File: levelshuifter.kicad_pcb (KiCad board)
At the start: 2 copper layers, 55 x 153 mm, 30 parts, among them J1 Screw_Terminal_01x02, J2 Conn_02x20_Odd_Even, J3 Conn_02x08_Odd_Even, J4 Conn_02x08_Odd_Even, J5 Conn_02x08_Odd_Even, U1 LM1117-3.3, U2 74LVC8T245PW, U3 74LVC8T245PW, U4 74LVC8T245PW, U5 L7805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

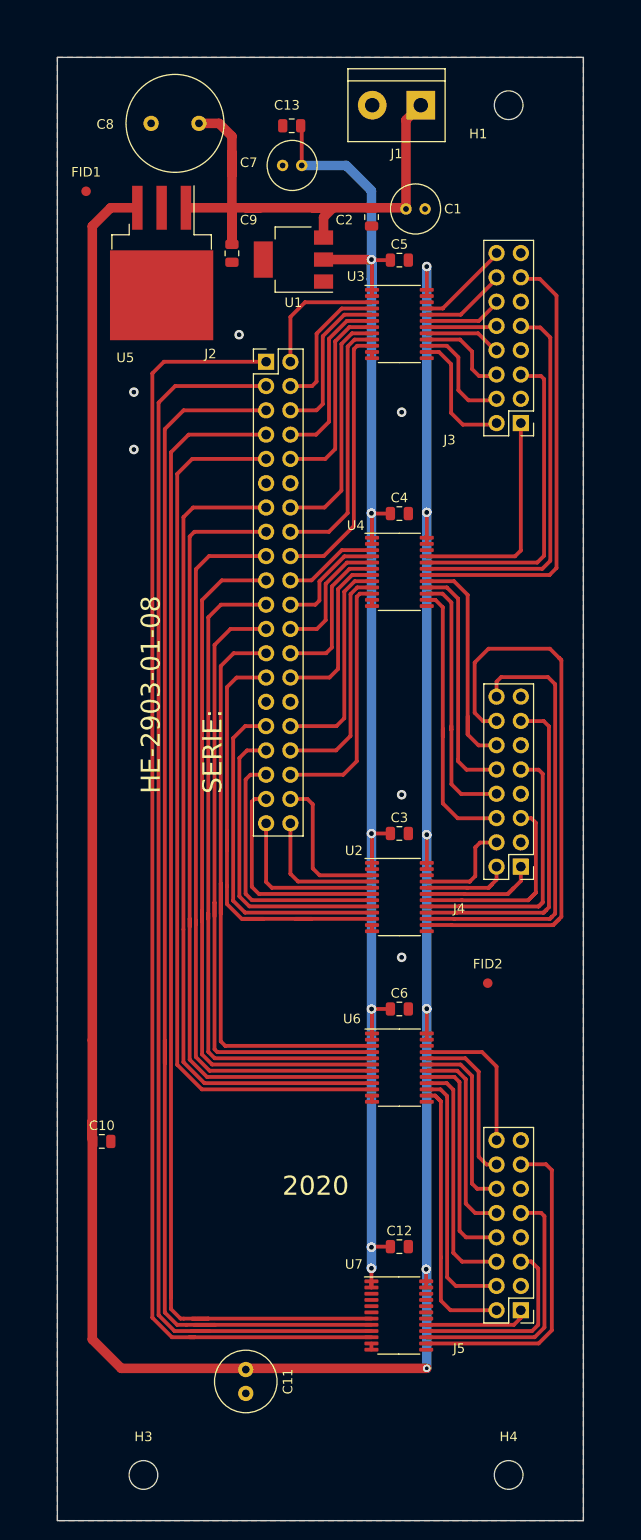
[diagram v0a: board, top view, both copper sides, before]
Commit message: sugerencias agregadas parcialmente
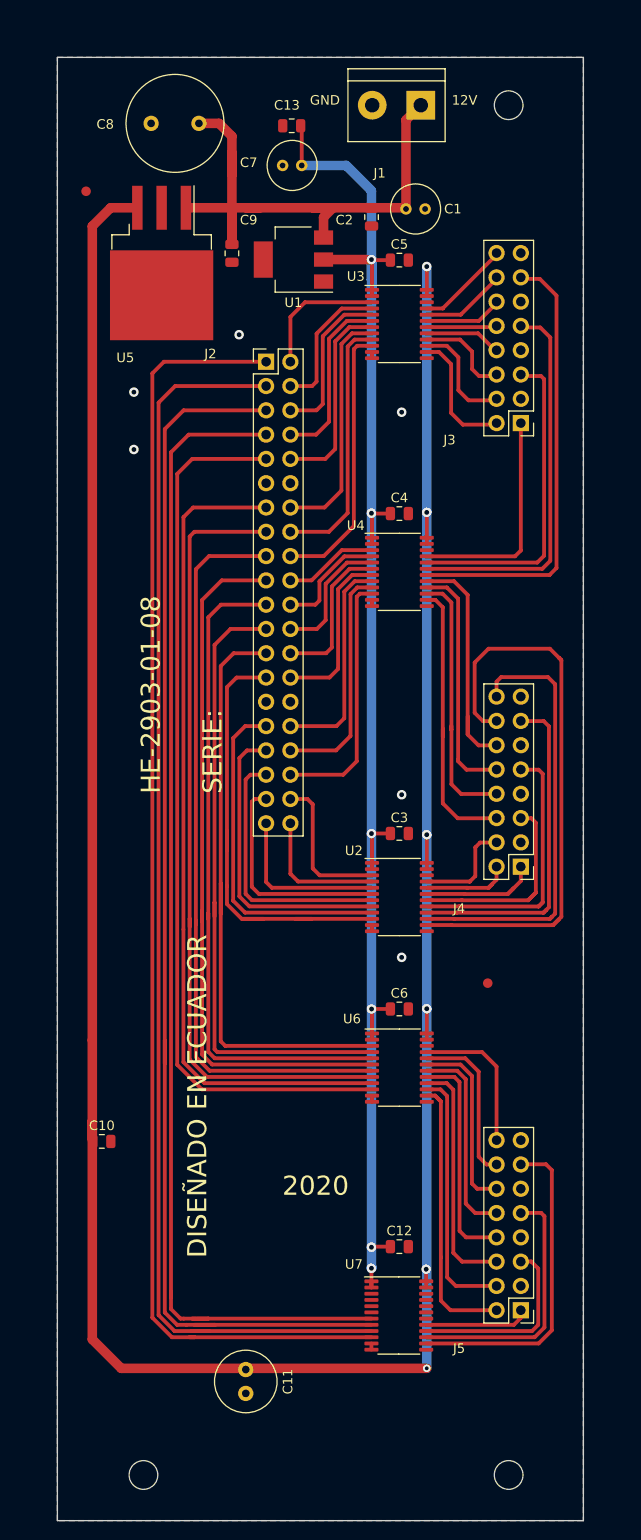
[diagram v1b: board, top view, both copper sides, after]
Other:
- board text added: "12V"
- board text added: "DISEÑADO EN ECUADOR"
- board text added: "GND"

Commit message: cambios 2
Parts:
- removed H4: MountingHole, MountingHole:MountingHole_3mm
- moved H3 7.22 mm to (35.0, 167.0)
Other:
- board size 55 x 153 mm -> 55 x 145 mm
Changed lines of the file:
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@@
   (general
     (thickness 1.6)
-    (drawings 13)
+    (drawings 12)
     (tracks 524)
     (zones 0)
-    (modules 30)
+    (modules 29)
     (nets 87)
   )
@@
   )
   (module MountingHole:MountingHole_3mm (layer F.Cu)
-    (at 73.185 174.224999)
-    (descr "Mounting Hole 3mm, no annular")
-    (tags "mounting hole 3mm no annular")
-    (attr virtual)
-    (fp_text reference H4 (at 0 -4) (layer F.SilkS) hide
-      (effects (font (size 1 1) (thickness 0.15)))
-    )
-    (fp_text value MountingHole (at 0 4) (layer F.Fab)
-      (effects (font (size 1 1) (thickness 0.15)))
-    )
-    (fp_circle (center 0 0) (end 3 0) (layer Cmts.User) (width 0.15))
-    (fp_circle (center 0 0) (end 3.25 0) (layer F.CrtYd) (width 0.05))
-    (fp_text user %R (at 0.3 0) (layer F.Fab)
-      (effects (font (size 1 1) (thickness 0.15)))
-    )
-    (pad 1 np_thru_hole circle (at 0 0) (size 3 3) (drill 3) (layers *.Cu *.Mask))
-  )
-  (module MountingHole:MountingHole_3mm (layer F.Cu)
-    (at 35 174.224999)
+    (at 35 167.005)
     (descr "Mounting Hole 3mm, no annular")
     (tags "mounting hole 3mm no annular")
@@
     )
   )
-  (gr_text "GND\n" (at 53.975 30.48) (layer F.SilkS)
-    (effects (font (size 1 1) (thickness 0.15)))
-  )
-  (gr_text "12V\n" (at 68.58 30.48) (layer F.SilkS)
-    (effects (font (size 1 1) (thickness 0.15)))
-  )
-  (gr_text "DISEÑADO EN ECUADOR" (at 40.64 134.62 90) (layer F.SilkS)
-    (effects (font (size 2 2) (thickness 0.15)))
-  )
-  (gr_text 2020 (at 53 144) (layer F.SilkS)
-    (effects (font (size 2 2) (thickness 0.15)))
-  )
-  (gr_text "HE-2903-01-08\n\nSERIE:" (at 39 103 90) (layer F.SilkS)
-    (effects (font (size 2 2) (thickness 0.15)) (justify left))
-  )
-  (gr_text "Fabricante seleccionado: Microcircuitos (Colombia)\nLimitaciones:\nhttps://pcbmicrocircuitos.com/wp-content/uploads/2016/12/medidas-minimas-microcircuitos-1.jpg\nDistancias:\n\ncobre-cobre: 0.203mm\nagujero-agujero:0.5mm\npads-serigraf:0.23mm\n\nAncho:\n\nPista:0.203mm\nVia:0.25mm\nSerigrafía:0.23mm\n\n" (at 102 50) (layer Dwgs.User)
-    (effects (font (size 2 2) (thickness 0.15)) (justify left))
-  )
   (dimension 55 (width 0.15) (layer Dwgs.User)
     (gr_text "55,000 mm" (at 53.5 18.7) (layer Dwgs.User)
@@
     (arrow2b (pts (xy 26 20) (xy 27.126504 19.413579)))
   )
-  (dimension 153 (width 0.15) (layer Dwgs.User)
-    (gr_text "153,000 mm" (at 92.3 102.5 270) (layer Dwgs.User)
-      (effects (font (size 1 1) (thickness 0.15)))
-    )
-    (feature1 (pts (xy 81 179) (xy 91.586421 179)))
-    (feature2 (pts (xy 81 26) (xy 91.586421 26)))
-    (crossbar (pts (xy 91 26) (xy 91 179)))
-    (arrow1a (pts (xy 91 179) (xy 90.413579 177.873496)))
-    (arrow1b (pts (xy 91 179) (xy 91.586421 177.873496)))
-    (arrow2a (pts (xy 91 26) (xy 90.413579 27.126504)))
-    (arrow2b (pts (xy 91 26) (xy 91.586421 27.126504)))
-  )
-  (gr_line (start 26 179) (end 26 26) (layer Edge.Cuts) (width 0.05))
-  (gr_line (start 81 178) (end 81 179) (layer Edge.Cuts) (width 0.05))
-  (gr_line (start 81 26) (end 81 178) (layer Edge.Cuts) (width 0.05))
+  (dimension 145 (width 0.15) (layer Dwgs.User)
+    (gr_text "145,000 mm" (at 87.3 98.5 270) (layer Dwgs.User)
+      (effects (font (size 1 1) (thickness 0.15)))
+    )
+    (feature1 (pts (xy 81 171) (xy 86.586421 171)))
+    (feature2 (pts (xy 81 26) (xy 86.586421 26)))
+    (crossbar (pts (xy 86 26) (xy 86 171)))
+    (arrow1a (pts (xy 86 171) (xy 85.413579 169.873496)))
+    (arrow1b (pts (xy 86 171) (xy 86.586421 169.873496)))
+    (arrow2a (pts (xy 86 26) (xy 85.413579 27.126504)))
+    (arrow2b (pts (xy 86 26) (xy 86.586421 27.126504)))
+  )
+  (gr_line (start 26 171) (end 26 26) (layer Edge.Cuts) (width 0.05))
+  (gr_line (start 26 171) (end 81 171) (layer Edge.Cuts) (width 0.05))
+  (gr_line (start 81 26) (end 81 171) (layer Edge.Cuts) (width 0.05))
   (gr_line (start 26 26) (end 81 26) (layer Edge.Cuts) (width 0.05))
-  (gr_line (start 81 179) (end 26 179) (layer Edge.Cuts) (width 0.05))
+  (gr_text "GND\n" (at 53.975 30.48) (layer F.SilkS)
+    (effects (font (size 1 1) (thickness 0.15)))
+  )
+  (gr_text "12V\n" (at 68.58 30.48) (layer F.SilkS)
+    (effects (font (size 1 1) (thickness 0.15)))
+  )
+  (gr_text "DISEÑADO EN ECUADOR" (at 40.64 134.62 90) (layer F.SilkS)
+    (effects (font (size 2 2) (thickness 0.15)))
+  )
+  (gr_text 2020 (at 53 144) (layer F.SilkS)
+    (effects (font (size 2 2) (thickness 0.15)))
+  )
+  (gr_text "HE-2903-01-08\n\nSERIE:" (at 39 103 90) (layer F.SilkS)
+    (effects (font (size 2 2) (thickness 0.15)) (justify left))
+  )
+  (gr_text "Fabricante seleccionado: Microcircuitos (Colombia)\nLimitaciones:\nhttps://pcbmicrocircuitos.com/wp-content/uploads/2016/12/medidas-minimas-microcircuitos-1.jpg\nDistancias:\n\ncobre-cobre: 0.203mm\nagujero-agujero:0.5mm\npads-serigraf:0.23mm\n\nAncho:\n\nPista:0.203mm\nVia:0.25mm\nSerigrafía:0.23mm\n\n" (at 102 50) (layer Dwgs.User)
+    (effects (font (size 2 2) (thickness 0.15)) (justify left))
+  )
   (segment (start 44.25 45.55) (end 44.25 42) (width 1) (layer F.Cu) (net 1))
   (segment (start 44.25 42) (end 44.525 41.725) (width 1) (layer F.Cu) (net 1))
@@
   (segment (start 70.4075 130.0075) (end 64.6225 130.0075) (width 0.4) (layer F.Cu) (net 78))
   (segment (start 71.92 131.52) (end 70.4075 130.0075) (width 0.4) (layer F.Cu) (net 78))
+  (zone (net 2) (net_name GND) (layer F.Cu) (hatch edge 0.508)
+    (connect_pads (clearance 0.254))
+    (min_thickness 0.254)
+    (fill yes (arc_segments 32) (thermal_gap 0.508) (thermal_bridge_width 0.508))
+    (polygon
+      (pts
+        (xy 83 173) (xy 24 173) (xy 24 24) (xy 83 24)
+      )
+    )
+  )
   (zone (net 2) (net_name GND) (layer B.Cu) (hatch edge 0.508)
     (connect_pads (clearance 0.254))
@@
     (polygon
       (pts
-        (xy 81 179) (xy 26 179) (xy 26 26) (xy 81 26)
+        (xy 85 175) (xy 22 175) (xy 22 22) (xy 85 22)
       )
     )
-  )
-  (zone (net 2) (net_name GND) (layer F.Cu) (hatch edge 0.508)
-    (connect_pads (clearance 0.25))
-    (min_thickness 0.254)
-    (fill yes (arc_segments 32) (thermal_gap 0.508) (thermal_bridge_width 0.508))
-    (polygon
-      (pts
-        (xy 81 179) (xy 26 179) (xy 26 26) (xy 81 26)
-      )
-    )

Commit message: cambios docu
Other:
- board text added: "Grilla: 1mm/0.01mm Vias: (0.80/0.40)mm y (1/0.5)mm Pistas: 0.40mm/1mm Margen: 0.25mm silkscreen: negro"
- board text removed: "Fabricante seleccionado: Microcircuitos (Colombia) Limitaciones: https://pcbmicrocircuitos.com/wp-content/uploads/2016/12/medidas-minimas-microcircuitos-1.jpg Distancias: cobre-cobre: 0.203mm agujero-agujero:0.5mm pads-serigraf:0.23mm Ancho: Pista:0.203mm Via:0.25mm Serigrafía:0.23mm"
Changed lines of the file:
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@@
     (effects (font (size 2 2) (thickness 0.15)) (justify left))
   )
-  (gr_text "Fabricante seleccionado: Microcircuitos (Colombia)\nLimitaciones:\nhttps://pcbmicrocircuitos.com/wp-content/uploads/2016/12/medidas-minimas-microcircuitos-1.jpg\nDistancias:\n\ncobre-cobre: 0.203mm\nagujero-agujero:0.5mm\npads-serigraf:0.23mm\n\nAncho:\n\nPista:0.203mm\nVia:0.25mm\nSerigrafía:0.23mm\n\n" (at 102 50) (layer Dwgs.User)
+  (gr_text "Grilla: 1mm/0.01mm\nVias: (0.80/0.40)mm y (1/0.5)mm\nPistas: 0.40mm/1mm\nMargen: 0.25mm\n\nsilkscreen: negro\n\n\n\n\n\n\n\n" (at 102 50) (layer Dwgs.User)
     (effects (font (size 2 2) (thickness 0.15)) (justify left))
   )

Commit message: nota de ultima
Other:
- board text added: "Grilla: 1mm/0.01mm Vias: (0.80/0.40)mm y (1/0.5)mm Pistas: 0.40mm/1mm Margen: 0.25mm Fabricación: FR4 silkscreen: negro"
- board text removed: "Grilla: 1mm/0.01mm Vias: (0.80/0.40)mm y (1/0.5)mm Pistas: 0.40mm/1mm Margen: 0.25mm silkscreen: negro"
